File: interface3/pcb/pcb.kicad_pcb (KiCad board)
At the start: 2 copper layers, 107.5 x 66 mm, 56 parts, among them J1 PORT1, J2 PORT2, J3 PORT3/4, J4 POWER, SW1 Pico Run, T1 78602/8JC, T2 78602/8JC, U1 DS34LV86T, U2 DS34LV87T, U3 Pico_W

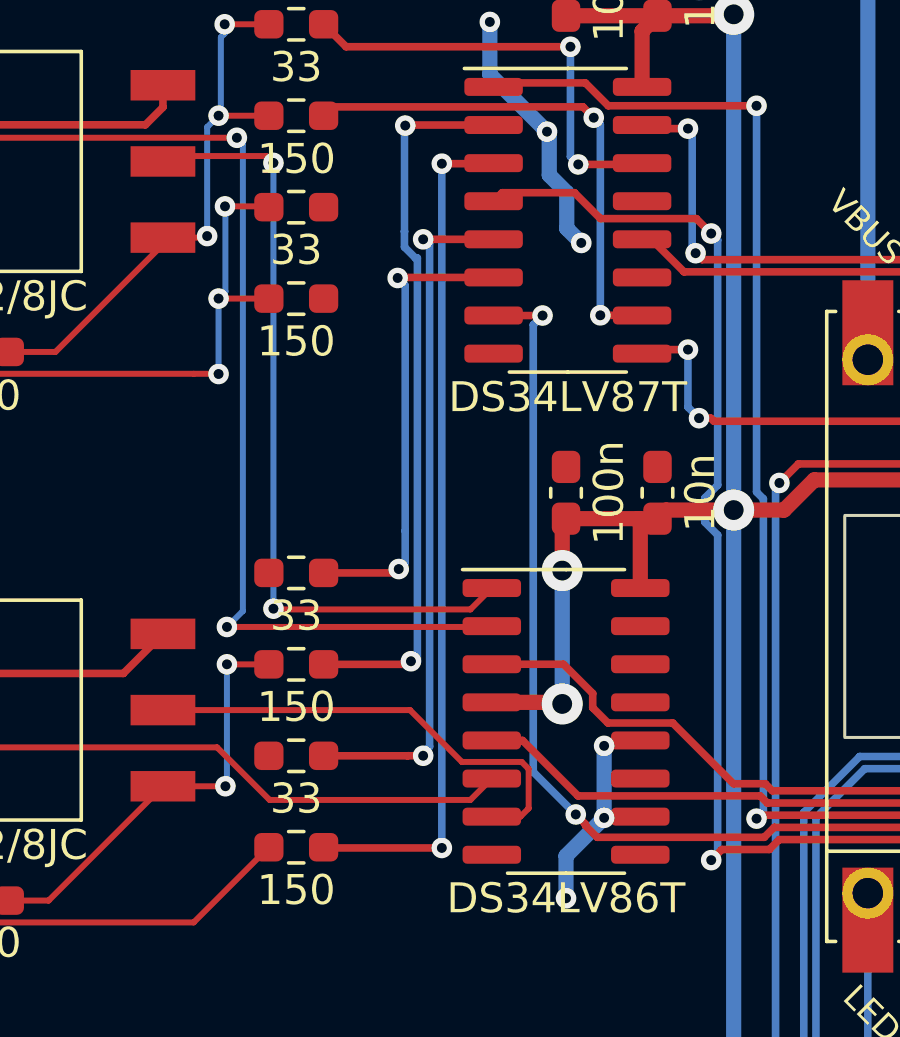
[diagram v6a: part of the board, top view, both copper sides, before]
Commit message: v2 sent to jlcpcb (with usb wiring)
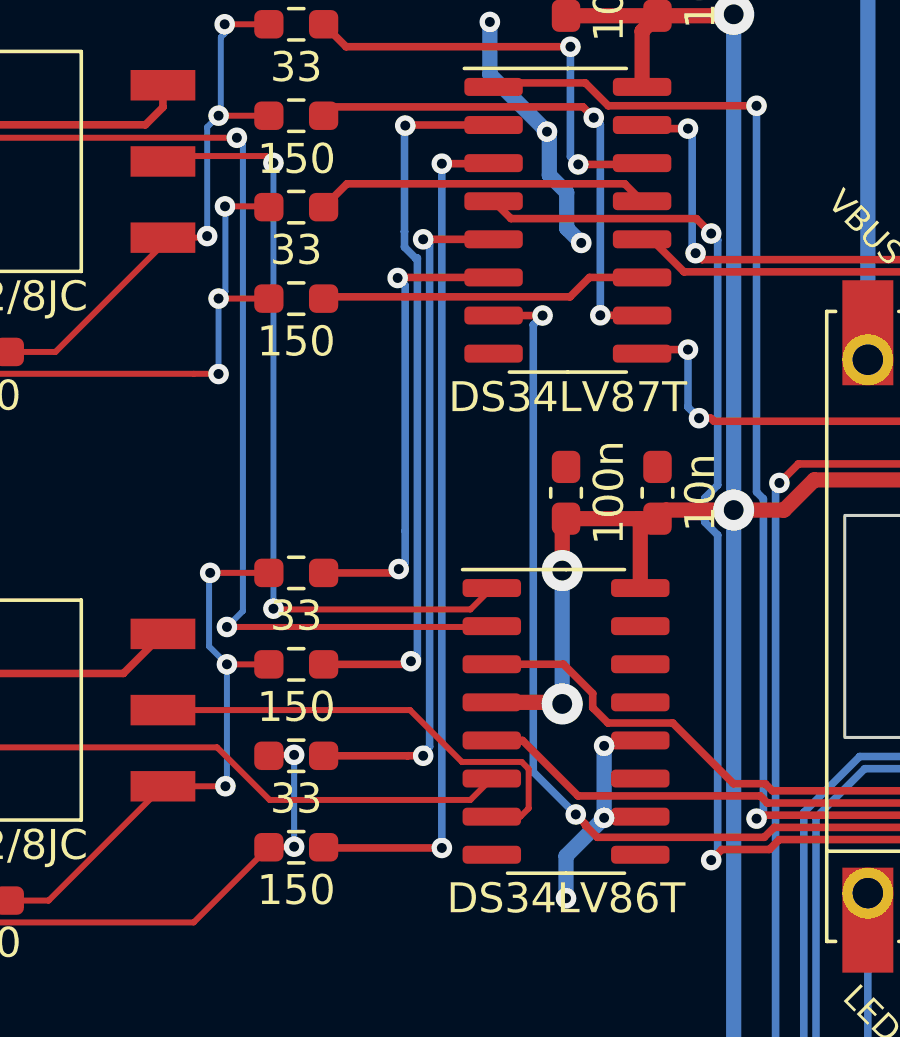
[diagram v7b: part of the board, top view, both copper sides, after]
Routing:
- net Net-(U2D-OUT-): track 0.00 -> 11.2 mm
- net Net-(U2C-OUT-): track 0.00 -> 10.9 mm
- net TX1-: track 14.3 -> 19.5 mm, vias 2 -> 3
- net TX1+: track 18.5 -> 23.3 mm, vias 0 -> 2
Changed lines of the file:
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@@
+	)
+	(segment
+		(start 145.857141 106.25)
+		(end 145.8762 106.230941)
+		(width 0.2)
+		(layer "F.Cu")
+		(net 42)
+	)
+	(segment
+		(start 145.065093 103.170907)
+		(end 145.034 103.202)
+		(width 0.2)
+		(layer "F.Cu")
+		(net 42)
+	)
+	(segment
+		(start 145.034 106.25)
+		(end 145.857141 106.25)
+		(width 0.2)
+		(layer "F.Cu")
+		(net 42)
 	)
 	(segment
@@
 	)
 	(segment
+		(start 145.8762 103.170907)
+		(end 145.065093 103.170907)
+		(width 0.2)
+		(layer "F.Cu")
+		(net 42)
+	)
+	(segment
 		(start 130.7484 104.218)
 		(end 134.5584 108.028)
@@
 		(net 42)
 	)
+	(via
+		(at 145.8762 103.170907)
+		(size 0.6858)
+		(drill 0.3302)
+		(layers "F.Cu" "B.Cu")
+		(net 42)
+	)
+	(via
+		(at 145.8762 106.230941)
+		(size 0.6858)
+		(drill 0.3302)
+		(layers "F.Cu" "B.Cu")
+		(net 42)
+	)
+	(segment
+		(start 145.8762 106.230941)
+		(end 145.8762 103.170907)
+		(width 0.2)
+		(layer "B.Cu")
+		(net 42)
+	)
+	(segment
+		(start 145.0322 97.1042)
+		(end 145.034 97.106)
+		(width 0.2)
+		(layer "F.Cu")
+		(net 43)
+	)
 	(segment
 		(start 141.5034 104.218)
@@
 	)
 	(segment
+		(start 143.0782 97.1042)
+		(end 145.0322 97.1042)
+		(width 0.2)
+		(layer "F.Cu")
+		(net 43)
+	)
+	(segment
 		(start 143.6388 100.154)
 		(end 143.637 100.1522)
@@
 	)
 	(via
+		(at 143.0782 97.1042)
+		(size 0.6858)
+		(drill 0.3302)
+		(layers "F.Cu" "B.Cu")
+		(net 43)
+	)
+	(via
 		(at 143.5862 104.2162)
 		(size 0.6858)
@@
 	)
 	(segment
+		(start 143.0407 97.1417)
+		(end 143.0782 97.1042)
+		(width 0.2)
+		(layer "B.Cu")
+		(net 43)
+	)
+	(segment
+		(start 143.0407 99.5559)
+		(end 143.0407 97.1417)
+		(width 0.2)
+		(layer "B.Cu")
+		(net 43)
+	)
+	(segment
 		(start 143.637 104.1654)
 		(end 143.637 100.1522)
@@
 	)
 	(segment
+		(start 143.637 100.1522)
+		(end 143.0407 99.5559)
+		(width 0.2)
+		(layer "B.Cu")
+		(net 43)
+	)
+	(segment
 		(start 145.0322 87.9602)
 		(end 145.034 87.962)
@@
 	)
 	(segment
+		(start 146.9183 87.9027)
+		(end 155.0737 87.9027)
+		(width 0.254)
+		(layer "F.Cu")
+		(net 45)
+	)
+	(segment
+		(start 146.859 87.962)
+		(end 146.9183 87.9027)
+		(width 0.254)
+		(layer "F.Cu")
+		(net 45)
+	)
+	(segment
+		(start 155.7204 87.256)
+		(end 157.475 87.256)
+		(width 0.254)
+		(layer "F.Cu")
+		(net 45)
+	)
+	(segment
+		(start 155.0737 87.9027)
+		(end 155.7204 87.256)
+		(width 0.254)
+		(layer "F.Cu")
+		(net 45)
+	)
+	(segment
 		(start 156.083 88.519)
 		(end 157.468 88.519)
@@
 	)
 	(segment
+		(start 156.8946 84.1356)
+		(end 147.6374 84.1356)
+		(width 0.254)
+		(layer "F.Cu")
+		(net 48)
+	)
+	(segment
+		(start 157.475 84.716)
+		(end 156.8946 84.1356)
+		(width 0.254)
+		(layer "F.Cu")
+		(net 48)
+	)
+	(segment
+		(start 147.6374 84.1356)
+		(end 146.859 84.914)
+		(width 0.254)
+		(layer "F.Cu")
+		(net 48)
+	)
+	(segment
 		(start 157.4312 83.4898)
 		(end 157.475 83.446)
@@
 	)
 	(segment
+		(start 153.1044 85.2954)
+		(end 152.525 84.716)
+		(width 0.254)
+		(layer "F.Cu")
+		(net 63)
+	)
+	(segment
 		(start 160.1343 106.3249)
 		(end 161.716102 106.3249)
@@
 	)
 	(segment
+		(start 159.281615 85.2954)
+		(end 153.1044 85.2954)
+		(width 0.254)
+		(layer "F.Cu")
+		(net 63)
+	)
+	(segment
 		(start 161.716102 106.3249)
 		(end 162.046802 105.9942)
@@
 	)
 	(segment
+		(start 159.7792 106.68)
+		(end 160.1343 106.3249)
+		(width 0.254)
+		(layer "F.Cu")
+		(net 63)
+	)
+	(segment
+		(start 175.002234 106.5403)
+		(end 176.4603 106.5403)
+		(width 0.254)
+		(layer "F.Cu")
+		(net 63)
+	)
+	(segment
 		(start 159.7792 85.792985)
 		(end 159.281615 85.2954)
@@
 	)
 	(segment
-		(start 159.7792 106.68)
-		(end 160.1343 106.3249)
-		(width 0.254)
-		(layer "F.Cu")
-		(net 63)
-	)
-	(segment
-		(start 175.002234 106.5403)
-		(end 176.4603 106.5403)
-		(width 0.254)
-		(layer "F.Cu")
-		(net 63)
-	)
-	(segment
-		(start 156.0852 85.2954)
-		(end 155.2216 84.4318)
-		(width 0.254)
-		(layer "F.Cu")
-		(net 63)
-	)
-	(segment
 		(start 171.910262 105.9942)
 		(end 172.240462 106.3244)
@@
 	)
 	(segment
-		(start 152.8092 84.4318)
-		(end 152.525 84.716)
-		(width 0.254)
-		(layer "F.Cu")
-		(net 63)
-	)
-	(segment
-		(start 159.281615 85.2954)
-		(end 156.0852 85.2954)
-		(width 0.254)
-		(layer "F.Cu")
-		(net 63)
-	)
-	(segment
 		(start 172.240462 106.3244)
 		(end 174.786334 106.3244)
@@
 		(width 0.254)
 		(layer "F.Cu")
-		(net 63)
-	)
-	(segment
-		(start 155.2216 84.4318)
-		(end 152.8092 84.4318)
-		(width 0.254)
-		(layer "F.Cu")
